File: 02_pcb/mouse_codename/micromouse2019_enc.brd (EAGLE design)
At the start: 5.9 x 11.1 mm, 7 parts, among them IC1 AS5047D-ATSM

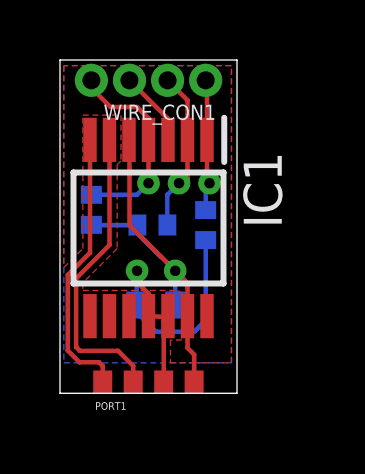
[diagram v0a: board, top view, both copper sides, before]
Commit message: Names and values on PCB arranged, values for R and C elements added
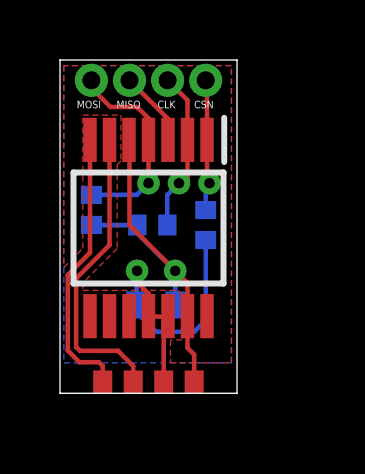
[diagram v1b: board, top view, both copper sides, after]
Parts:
- C1: value (none) -> 100n
- IC1: value AS5047D-ATSM -> AS5047D
- R1, R2, R3: value (none) -> 10k
- renumbered WIRE_CON1 to SPI
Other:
- board text added: "CLK"
- board text added: "CSN"
- board text added: "MISO"
- board text added: "MOSI"
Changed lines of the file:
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@@
 <setting verticaltext="up"/>
 </settings>
-<grid distance="5" unitdist="mil" unit="mil" style="lines" multiple="1" display="yes" altdistance="0.1" altunitdist="mil" altunit="mil"/>
+<grid distance="1" unitdist="mil" unit="mm" style="lines" multiple="1" display="yes" altdistance="0.1" altunitdist="mil" altunit="mil"/>
 <layers>
 <layer number="1" name="Top" color="4" fill="1" visible="yes" active="yes"/>
@@
 <layer number="27" name="tValues" color="7" fill="1" visible="yes" active="yes"/>
 <layer number="28" name="bValues" color="7" fill="1" visible="yes" active="yes"/>
-<layer number="29" name="tStop" color="7" fill="3" visible="no" active="yes"/>
-<layer number="30" name="bStop" color="7" fill="6" visible="no" active="yes"/>
-<layer number="31" name="tCream" color="7" fill="4" visible="no" active="yes"/>
-<layer number="32" name="bCream" color="7" fill="5" visible="no" active="yes"/>
+<layer number="29" name="tStop" color="7" fill="3" visible="yes" active="yes"/>
+<layer number="30" name="bStop" color="7" fill="6" visible="yes" active="yes"/>
+<layer number="31" name="tCream" color="7" fill="4" visible="yes" active="yes"/>
+<layer number="32" name="bCream" color="7" fill="5" visible="yes" active="yes"/>
 <layer number="33" name="tFinish" color="6" fill="3" visible="yes" active="yes"/>
 <layer number="34" name="bFinish" color="6" fill="6" visible="yes" active="yes"/>
-<layer number="35" name="tGlue" color="7" fill="4" visible="no" active="yes"/>
-<layer number="36" name="bGlue" color="7" fill="5" visible="no" active="yes"/>
-<layer number="37" name="tTest" color="7" fill="1" visible="no" active="yes"/>
-<layer number="38" name="bTest" color="7" fill="1" visible="no" active="yes"/>
+<layer number="35" name="tGlue" color="7" fill="4" visible="yes" active="yes"/>
+<layer number="36" name="bGlue" color="7" fill="5" visible="yes" active="yes"/>
+<layer number="37" name="tTest" color="7" fill="1" visible="yes" active="yes"/>
+<layer number="38" name="bTest" color="7" fill="1" visible="yes" active="yes"/>
 <layer number="39" name="tKeepout" color="4" fill="11" visible="yes" active="yes"/>
 <layer number="40" name="bKeepout" color="1" fill="11" visible="yes" active="yes"/>
@@
 <dimension x1="2.95" y1="5.51" x2="0" y2="5.51" x3="1.475" y3="23.41" textsize="1.778" layer="47" dtype="horizontal" width="0.05" extwidth="0.01" extlength="2" precision="3"/>
 <dimension x1="5.9" y1="0" x2="5.9" y2="11.11" x3="11.58" y3="5.555" textsize="1.778" layer="47" dtype="horizontal" width="0.05" extwidth="0.01" extlength="2" precision="3"/>
+<text x="1.8796" y="9.4996" size="0.254" layer="25">MISO</text>
+<text x="0.5588" y="9.4996" size="0.254" layer="25">MOSI</text>
+<text x="3.2512" y="9.4996" size="0.254" layer="25">CLK</text>
+<text x="4.4704" y="9.4996" size="0.254" layer="25">CSN</text>
 </plain>
 <attributes>
@@
 </autorouter>
 <elements>
-<element name="IC1" library="parts_not_managed" package="SOP65P640X120-14N" value="AS5047D-ATSM" x="2.95" y="5.51" smashed="yes" rot="R270">
+<element name="IC1" library="parts_not_managed" package="SOP65P640X120-14N" value="AS5047D" x="2.95" y="5.51" smashed="yes" rot="R270">
 <attribute name="DESCRIPTION" value="ams AS5047D-ATSM Hall Effect Sensor 14-Pin TSSOP, 3  3.6 V, 4.5  5.5 V" x="2.95" y="5.51" size="1.778" layer="27" rot="R270" display="off"/>
 <attribute name="HEIGHT" value="1.2mm" x="2.95" y="5.51" size="1.778" layer="27" rot="R270" display="off"/>
@@
 <attribute name="MOUSER_PART_NUMBER" value="985-AS5047D-ATSM" x="2.95" y="5.51" size="1.778" layer="27" rot="R270" display="off"/>
 <attribute name="MOUSER_PRICE-STOCK" value="https://www.mouser.com/Search/Refine.aspx?Keyword=985-AS5047D-ATSM" x="2.95" y="5.51" size="1.778" layer="27" rot="R270" display="off"/>
-<attribute name="NAME" x="6.76" y="6.78" size="1.27" layer="25" rot="R270" align="center"/>
 <attribute name="RS_PART_NUMBER" value="1700756" x="2.95" y="5.51" size="1.778" layer="27" rot="R270" display="off"/>
 <attribute name="RS_PRICE-STOCK" value="http://uk.rs-online.com/web/p/products/1700756" x="2.95" y="5.51" size="1.778" layer="27" rot="R270" display="off"/>
-<attribute name="VALUE" x="-0.86" y="6.78" size="1.27" layer="27" rot="R270" align="center"/>
+<attribute name="VALUE" x="2.999" y="1.3244" size="0.7" layer="27" align="center"/>
 </element>
-<element name="R1" library="rcl" library_urn="urn:adsk.eagle:library:334" package="R0402" package3d_urn="urn:adsk.eagle:package:23547/3" value="" x="4.8560375" y="5.60658125" smashed="yes" rot="MR270">
-<attribute name="NAME" x="4.2210375" y="6.24158125" size="1.27" layer="26" rot="MR270"/>
+<element name="R1" library="rcl" library_urn="urn:adsk.eagle:library:334" package="R0402" package3d_urn="urn:adsk.eagle:package:23547/3" value="10k" x="4.8560375" y="5.60658125" smashed="yes" rot="MR270">
+<attribute name="NAME" x="4.395934375" y="9.21975625" size="0.7" layer="26" rot="MR180"/>
 <attribute name="SPICEPREFIX" value="R" x="4.8560375" y="5.60658125" size="1.778" layer="28" rot="MR270" display="off"/>
-<attribute name="VALUE" x="6.7610375" y="6.24158125" size="1.27" layer="28" rot="MR270"/>
+<attribute name="VALUE" x="4.14701875" y="8.2342375" size="0.7" layer="28" rot="MR180"/>
 </element>
-<element name="R2" library="rcl" library_urn="urn:adsk.eagle:library:334" package="R0402" package3d_urn="urn:adsk.eagle:package:23547/3" value="" x="3.0780375" y="5.60658125" smashed="yes" rot="MR180">
-<attribute name="NAME" x="2.4430375" y="4.97158125" size="1.27" layer="26" rot="MR180"/>
+<element name="R2" library="rcl" library_urn="urn:adsk.eagle:library:334" package="R0402" package3d_urn="urn:adsk.eagle:package:23547/3" value="10k" x="3.0780375" y="5.60658125" smashed="yes" rot="MR180">
+<attribute name="NAME" x="3.6783625" y="8.51581875" size="0.7" layer="26" rot="MR0"/>
 <attribute name="SPICEPREFIX" value="R" x="3.0780375" y="5.60658125" size="1.778" layer="28" rot="MR180" display="off"/>
-<attribute name="VALUE" x="2.4430375" y="7.51158125" size="1.27" layer="28" rot="MR180"/>
+<attribute name="VALUE" x="3.78504375" y="7.525215625" size="0.7" layer="28" rot="MR0"/>
 </element>
-<element name="R3" library="rcl" library_urn="urn:adsk.eagle:library:334" package="R0402" package3d_urn="urn:adsk.eagle:package:23547/3" value="" x="1.0460375" y="6.11458125" smashed="yes" rot="MR90">
-<attribute name="NAME" x="1.6810375" y="5.47958125" size="1.27" layer="26" rot="MR90"/>
+<element name="R3" library="rcl" library_urn="urn:adsk.eagle:library:334" package="R0402" package3d_urn="urn:adsk.eagle:package:23547/3" value="10k" x="1.0460375" y="6.11458125" smashed="yes" rot="MR90">
+<attribute name="NAME" x="1.77211875" y="8.49585625" size="0.7" layer="26" rot="MR0"/>
 <attribute name="SPICEPREFIX" value="R" x="1.0460375" y="6.11458125" size="1.778" layer="28" rot="MR90" display="off"/>
-<attribute name="VALUE" x="-0.8589625" y="5.47958125" size="1.27" layer="28" rot="MR90"/>
+<attribute name="VALUE" x="1.868640625" y="7.528115625" size="0.7" layer="28" rot="MR0"/>
 </element>
-<element name="C1" library="rcl" library_urn="urn:adsk.eagle:library:334" package="C0402" package3d_urn="urn:adsk.eagle:package:23626/2" value="" x="3.2050375" y="2.93958125" smashed="yes" rot="MR180">
-<attribute name="NAME" x="2.5700375" y="2.30458125" size="1.27" layer="26" rot="MR180"/>
+<element name="C1" library="rcl" library_urn="urn:adsk.eagle:library:334" package="C0402" package3d_urn="urn:adsk.eagle:package:23626/2" value="100n" x="3.2050375" y="2.93958125" smashed="yes" rot="MR180">
+<attribute name="NAME" x="0.3856375" y="3.21898125" size="0.7" layer="26" rot="MR180"/>
 <attribute name="SPICEPREFIX" value="C" x="3.2050375" y="2.93958125" size="1.778" layer="28" rot="MR180" display="off"/>
-<attribute name="VALUE" x="2.5700375" y="4.84458125" size="1.27" layer="28" rot="MR180"/>
+<attribute name="VALUE" x="0.3856375" y="2.22838125" size="0.7" layer="28" rot="MR180"/>
 </element>
-<element name="PORT1" library="parts_not_managed" package="ENC_PORT_MODULE" value="ENC_PORT_MODULE" x="2.948496875" y="0.380921875" smashed="yes">
-<attribute name="NAME" x="1.170496875" y="-0.5504125" size="0.254" layer="25"/>
-<attribute name="VALUE" x="1.170496875" y="-0.97374375" size="0.254" layer="27"/>
-</element>
-<element name="WIRE_CON1" library="parts_not_managed" package="PINHD4-1.27" value="CON_WIRE" x="2.9510375" y="10.43258125" smashed="yes" rot="R180">
-<attribute name="NAME" x="5.2020375" y="9.620915625" size="0.508" layer="25" rot="R180"/>
-</element>
+<element name="PORT1" library="parts_not_managed" package="ENC_PORT_MODULE" value="ENC_PORT_MODULE" x="2.948496875" y="0.380921875" smashed="yes"/>
+<element name="SPI" library="parts_not_managed" package="PINHD4-1.27" value="CON_WIRE" x="2.9510375" y="10.43258125" smashed="yes" rot="R180"/>
 </elements>
 <signals>
@@
 <contactref element="IC1" pad="2"/>
 <contactref element="R2" pad="2"/>
-<contactref element="WIRE_CON1" pad="P2"/>
+<contactref element="SPI" pad="P2"/>
 <wire x1="4.25" y1="8.448" x2="4.2510375" y2="7.16058125" width="0.1524" layer="1"/>
 <wire x1="4.2510375" y1="7.16058125" x2="4.0940375" y2="7.00358125" width="0.1524" layer="1"/>
@@
 </signal>
 <signal name="CSN">
-<contactref element="WIRE_CON1" pad="P1"/>
+<contactref element="SPI" pad="P1"/>
 <contactref element="IC1" pad="1"/>
 <contactref element="R1" pad="1"/>
@@
 </signal>
 <signal name="MISO">
-<contactref element="WIRE_CON1" pad="P3"/>
+<contactref element="SPI" pad="P3"/>
 <contactref element="IC1" pad="3"/>
 <wire x1="3.6" y1="8.448" x2="3.6010375" y2="9.14758125" width="0.1524" layer="1"/>
@@
 </signal>
 <signal name="MOSI">
-<contactref element="WIRE_CON1" pad="P4"/>
+<contactref element="SPI" pad="P4"/>
 <contactref element="IC1" pad="4"/>
 <contactref element="R3" pad="2"/>

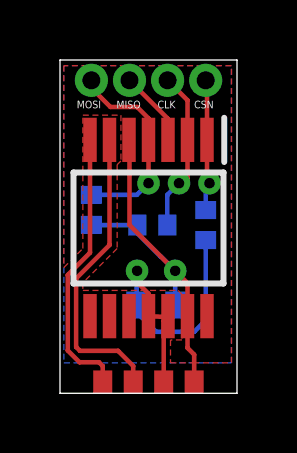
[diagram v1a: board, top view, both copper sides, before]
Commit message: increased size of enc port smds
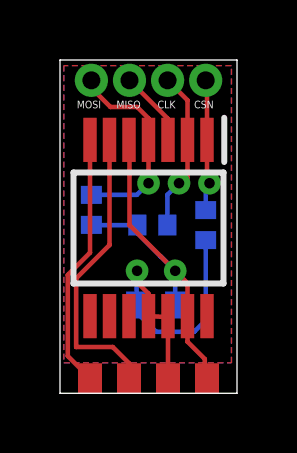
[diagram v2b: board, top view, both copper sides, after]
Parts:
- moved PORT1 0.12 mm to (2.95, 0.50)
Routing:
- net B: track 9.24 -> 8.56 mm
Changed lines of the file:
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@@
 <setting verticaltext="up"/>
 </settings>
-<grid distance="1" unitdist="mil" unit="mm" style="lines" multiple="1" display="yes" altdistance="0.1" altunitdist="mil" altunit="mil"/>
+<grid distance="5" unitdist="mil" unit="mil" style="lines" multiple="1" display="yes" altdistance="0.1" altunitdist="mil" altunit="mil"/>
 <layers>
 <layer number="1" name="Top" color="4" fill="1" visible="yes" active="yes"/>
@@
 <param name="mdSmdPad" value="6mil"/>
 <param name="mdSmdVia" value="6mil"/>
-<param name="mdSmdSmd" value="6mil"/>
+<param name="mdSmdSmd" value="5mil"/>
 <param name="mdViaViaSameLayer" value="6mil"/>
 <param name="mnLayersViaInSmd" value="2"/>
@@
 <attribute name="VALUE" x="0.3856375" y="2.22838125" size="0.7" layer="28" rot="MR180"/>
 </element>
-<element name="PORT1" library="parts_not_managed" package="ENC_PORT_MODULE" value="ENC_PORT_MODULE" x="2.948496875" y="0.380921875" smashed="yes"/>
 <element name="SPI" library="parts_not_managed" package="PINHD4-1.27" value="CON_WIRE" x="2.9510375" y="10.43258125" smashed="yes" rot="R180"/>
+<element name="PORT1" library="parts_not_managed" package="ENC_PORT_MODULE" value="ENC_PORT_MODULE" x="2.95" y="0.5" smashed="yes">
+<attribute name="VALUE" x="0.45" y="-0.931665625" size="0.7" layer="27"/>
+</element>
 </elements>
 <signals>
@@
 <contactref element="IC1" pad="12"/>
 <contactref element="C1" pad="1"/>
-<contactref element="PORT1" pad="P3"/>
 <wire x1="2.95" y1="2.572" x2="3.5860375" y2="2.54158125" width="0.1524" layer="1"/>
 <wire x1="3.5860375" y1="2.54158125" x2="3.6" y2="2.572" width="0.1524" layer="1"/>
@@
 <wire x1="4.8560375" y1="2.43158125" x2="4.8560375" y2="5.10658125" width="0.1524" layer="16"/>
 <wire x1="3.2050375" y1="2.05058125" x2="4.4750375" y2="2.05058125" width="0.1524" layer="16"/>
-<wire x1="3.456496875" y1="0.380921875" x2="3.456496875" y2="2.412040625" width="0.1524" layer="1"/>
-<wire x1="3.456496875" y1="2.412040625" x2="3.5860375" y2="2.54158125" width="0.1524" layer="1"/>
+<contactref element="PORT1" pad="P3"/>
+<wire x1="3.6" y1="0.5" x2="3.6" y2="2.52761875" width="0.1524" layer="1"/>
+<wire x1="3.6" y1="2.52761875" x2="3.5860375" y2="2.54158125" width="0.1524" layer="1"/>
 </signal>
 <signal name="CLK">
@@
 <contactref element="IC1" pad="5"/>
 <contactref element="C1" pad="2"/>
-<contactref element="PORT1" pad="P4"/>
 <wire x1="4.25" y1="2.572" x2="4.2510375" y2="3.67158125" width="0.1524" layer="1"/>
 <wire x1="2.3160375" y1="5.60658125" x2="2.3160375" y2="8.40258125" width="0.1524" layer="1"/>
@@
 <wire x1="2.5780375" y1="5.60658125" x2="2.5780375" y2="5.33044375" width="0.1524" layer="16"/>
 <wire x1="2.5780375" y1="5.33044375" x2="3.3433" y2="4.56518125" width="0.1524" layer="16"/>
-<wire x1="4.472496875" y1="0.380921875" x2="4.472496875" y2="1.291121875" width="0.1524" layer="1"/>
-<wire x1="4.2510375" y1="1.51258125" x2="4.25" y2="2.572" width="0.1524" layer="1"/>
-<wire x1="4.472496875" y1="1.291121875" x2="4.2510375" y2="1.51258125" width="0.1524" layer="1"/>
-<polygon width="0.1524" layer="1">
-<vertex x="4.445" y="1.016"/>
+<polygon width="0.1524" layer="16">
+<vertex x="0.127" y="10.922"/>
+<vertex x="0.127" y="1.016"/>
 <vertex x="5.715" y="1.016"/>
 <vertex x="5.715" y="10.922"/>
-<vertex x="0.127" y="10.922"/>
-<vertex x="0.127" y="4.191"/>
-<vertex x="0.762" y="4.826"/>
-<vertex x="0.762" y="9.271"/>
-<vertex x="2.032" y="9.271"/>
-<vertex x="2.032" y="7.747"/>
-<vertex x="1.905" y="7.62"/>
-<vertex x="1.905" y="4.826"/>
-<vertex x="0.762" y="3.683"/>
-<vertex x="0.762" y="3.429"/>
-<vertex x="3.937" y="3.429"/>
-<vertex x="4.064" y="3.302"/>
-<vertex x="4.064" y="1.778"/>
-<vertex x="3.683" y="1.778"/>
-<vertex x="3.683" y="1.016"/>
 </polygon>
-<polygon width="0.1524" layer="16">
+<contactref element="PORT1" pad="P4"/>
+<wire x1="4.9" y1="0.5" x2="4.826" y2="0.574" width="0.1524" layer="1"/>
+<wire x1="4.826" y1="0.574" x2="4.826" y2="1.143" width="0.1524" layer="1"/>
+<wire x1="4.25" y1="1.719" x2="4.25" y2="2.572" width="0.1524" layer="1"/>
+<wire x1="4.826" y1="1.143" x2="4.25" y2="1.719" width="0.1524" layer="1"/>
+<polygon width="0.1524" layer="1">
 <vertex x="0.127" y="10.922"/>
 <vertex x="0.127" y="1.016"/>
@@
 <signal name="A">
 <contactref element="IC1" pad="6"/>
-<contactref element="PORT1" pad="P2"/>
 <wire x1="1.65" y1="8.448" x2="1.6510375" y2="4.94158125" width="0.1524" layer="1"/>
 <wire x1="0.5380375" y1="3.82858125" x2="0.5380375" y2="1.54258125" width="0.1524" layer="1"/>
-<wire x1="0.5380375" y1="1.54258125" x2="0.6650375" y2="1.41558125" width="0.1524" layer="1"/>
-<wire x1="1.9350375" y1="1.41558125" x2="2.440496875" y2="0.910121875" width="0.1524" layer="1"/>
-<wire x1="2.440496875" y1="0.910121875" x2="2.440496875" y2="0.380921875" width="0.1524" layer="1"/>
 <wire x1="1.6510375" y1="4.94158125" x2="0.5380375" y2="3.82858125" width="0.1524" layer="1"/>
-<wire x1="0.6650375" y1="1.41558125" x2="1.9350375" y2="1.41558125" width="0.1524" layer="1"/>
+<contactref element="PORT1" pad="P2"/>
+<wire x1="0.5380375" y1="1.54258125" x2="1.75941875" y2="1.54258125" width="0.1524" layer="1"/>
+<wire x1="2.3" y1="1.002" x2="2.3" y2="0.5" width="0.1524" layer="1"/>
+<wire x1="1.75941875" y1="1.54258125" x2="2.3" y2="1.002" width="0.1524" layer="1"/>
 </signal>
 <signal name="B">
 <contactref element="IC1" pad="7"/>
+<wire x1="1" y1="8.448" x2="1.0010375" y2="4.68671875" width="0.1524" layer="1"/>
+<wire x1="1.0010375" y1="4.68671875" x2="0.2586375" y2="3.94431875" width="0.1524" layer="1"/>
 <contactref element="PORT1" pad="P1"/>
-<wire x1="1" y1="8.448" x2="1.0010375" y2="4.68671875" width="0.1524" layer="1"/>
-<wire x1="0.2586375" y1="3.94431875" x2="0.2586375" y2="1.42684375" width="0.1524" layer="1"/>
-<wire x1="1.0010375" y1="4.68671875" x2="0.2586375" y2="3.94431875" width="0.1524" layer="1"/>
-<wire x1="1.3000375" y1="1.03458125" x2="1.424496875" y2="0.910121875" width="0.1524" layer="1"/>
-<wire x1="1.424496875" y1="0.910121875" x2="1.424496875" y2="0.380921875" width="0.1524" layer="1"/>
-<wire x1="0.2586375" y1="1.42684375" x2="0.6509" y2="1.03458125" width="0.1524" layer="1"/>
-<wire x1="0.6509" y1="1.03458125" x2="1.3000375" y2="1.03458125" width="0.1524" layer="1"/>
+<wire x1="0.2586375" y1="1.2413625" x2="1" y2="0.5" width="0.1524" layer="1"/>
+<wire x1="0.2586375" y1="3.94431875" x2="0.2586375" y2="1.2413625" width="0.1524" layer="1"/>
 </signal>
 <signal name="CSN">
